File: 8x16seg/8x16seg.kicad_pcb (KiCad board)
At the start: 4 copper layers, 162.2 x 30.5 mm, 76 parts, among them P1 CONN_01X08, P2 CONN_01X08, U1 TLC59282_REV, U2 TLC59282_REV, U3 TLC59282_REV, U4 TLC59282_REV, U5 TLC59282_REV, U6 TLC59282_REV, U7 TLC59282_REV, U8 TLC59282_REV, U9 TLC59282_REV

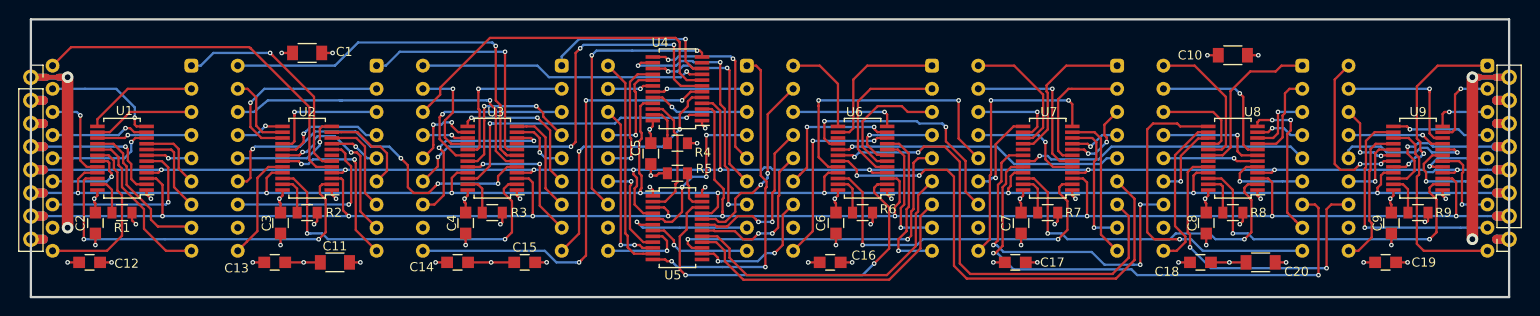
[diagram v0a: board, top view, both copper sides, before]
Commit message: Update LED module footprint to point to the 3D model.
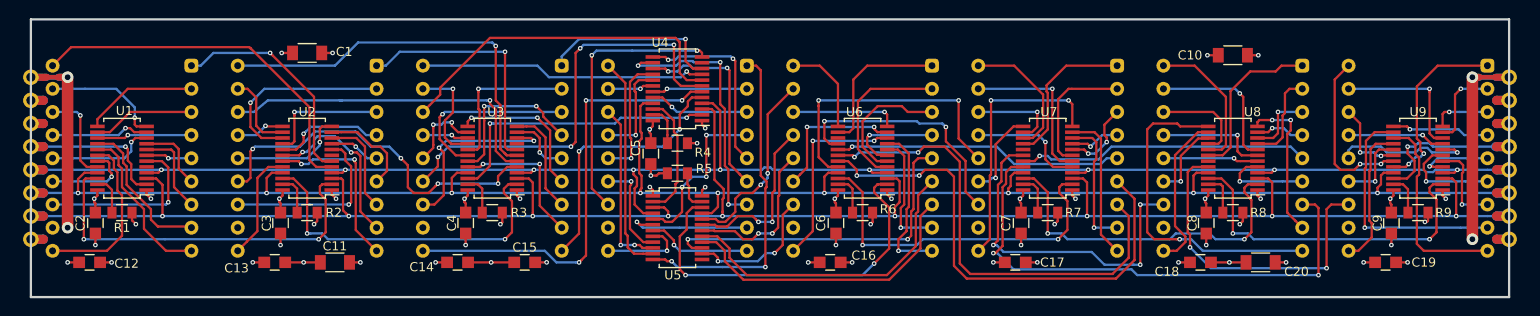
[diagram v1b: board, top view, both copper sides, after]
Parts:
- removed the REF** at (227.1, 97.8) (x2)
- removed the REF** at (227.1, 100.3) (x2)
- removed the REF** at (227.1, 102.9) (x2)
- removed the REF** at (227.1, 105.4) (x2)
- removed the REF** at (227.1, 108.0) (x2)
- removed the REF** at (227.1, 110.5) (x2)
- removed the REF** at (67.6, 110.5) (x2)
- removed the REF** at (227.1, 95.2) (x2)
- removed the REF** at (67.6, 108.0) (x2)
- removed the REF** at (67.6, 105.4) (x2)
- removed the REF** at (67.6, 102.9) (x2)
- removed the REF** at (67.6, 100.3) (x2)
- removed the REF** at (67.6, 97.8) (x2)
- added REF**: TestPoint_Pad_D1.0mm, TestPoint:TestPoint_Pad_D1.0mm, B.Cu at (227.1, 97.8)
- added REF**: TestPoint_Pad_D1.0mm, TestPoint:TestPoint_Pad_D1.0mm, B.Cu at (227.1, 100.3)
- added REF**: TestPoint_Pad_D1.0mm, TestPoint:TestPoint_Pad_D1.0mm, B.Cu at (227.1, 102.9)
- added REF**: TestPoint_Pad_D1.0mm, TestPoint:TestPoint_Pad_D1.0mm, B.Cu at (227.1, 105.4)
- added REF**: TestPoint_Pad_D1.0mm, TestPoint:TestPoint_Pad_D1.0mm, B.Cu at (227.1, 108.0)
- added REF**: TestPoint_Pad_D1.0mm, TestPoint:TestPoint_Pad_D1.0mm, B.Cu at (227.1, 110.5)
- added REF**: TestPoint_Pad_D1.0mm, TestPoint:TestPoint_Pad_D1.0mm, F.Cu at (227.1, 110.5)
- added REF**: TestPoint_Pad_D1.0mm, TestPoint:TestPoint_Pad_D1.0mm, F.Cu at (227.1, 108.0)
- added REF**: TestPoint_Pad_D1.0mm, TestPoint:TestPoint_Pad_D1.0mm, F.Cu at (227.1, 105.4)
- added REF**: TestPoint_Pad_D1.0mm, TestPoint:TestPoint_Pad_D1.0mm, F.Cu at (227.1, 102.9)
- added REF**: TestPoint_Pad_D1.0mm, TestPoint:TestPoint_Pad_D1.0mm, B.Cu at (67.6, 110.5)
- added REF**: TestPoint_Pad_D1.0mm, TestPoint:TestPoint_Pad_D1.0mm, F.Cu at (227.1, 100.3)
- added REF**: TestPoint_Pad_D1.0mm, TestPoint:TestPoint_Pad_D1.0mm, F.Cu at (227.1, 97.8)
- added REF**: TestPoint_Pad_D1.0mm, TestPoint:TestPoint_Pad_D1.0mm, F.Cu at (227.1, 95.2)
- added REF**: TestPoint_Pad_D1.0mm, TestPoint:TestPoint_Pad_D1.0mm, F.Cu at (67.6, 110.5)
- added REF**: TestPoint_Pad_D1.0mm, TestPoint:TestPoint_Pad_D1.0mm, F.Cu at (67.6, 108.0)
- added REF**: TestPoint_Pad_D1.0mm, TestPoint:TestPoint_Pad_D1.0mm, F.Cu at (67.6, 105.4)
- added REF**: TestPoint_Pad_D1.0mm, TestPoint:TestPoint_Pad_D1.0mm, F.Cu at (67.6, 102.9)
- added REF**: TestPoint_Pad_D1.0mm, TestPoint:TestPoint_Pad_D1.0mm, F.Cu at (67.6, 100.3)
- added REF**: TestPoint_Pad_D1.0mm, TestPoint:TestPoint_Pad_D1.0mm, F.Cu at (67.6, 97.8)
- added REF**: TestPoint_Pad_D1.0mm, TestPoint:TestPoint_Pad_D1.0mm, B.Cu at (67.6, 108.0)
- added REF**: TestPoint_Pad_D1.0mm, TestPoint:TestPoint_Pad_D1.0mm, B.Cu at (67.6, 105.4)
- added REF**: TestPoint_Pad_D1.0mm, TestPoint:TestPoint_Pad_D1.0mm, B.Cu at (67.6, 102.9)
- added REF**: TestPoint_Pad_D1.0mm, TestPoint:TestPoint_Pad_D1.0mm, B.Cu at (67.6, 100.3)
- added REF**: TestPoint_Pad_D1.0mm, TestPoint:TestPoint_Pad_D1.0mm, B.Cu at (67.6, 97.8)
- added REF**: TestPoint_Pad_D1.0mm, TestPoint:TestPoint_Pad_D1.0mm, B.Cu at (227.1, 95.2)

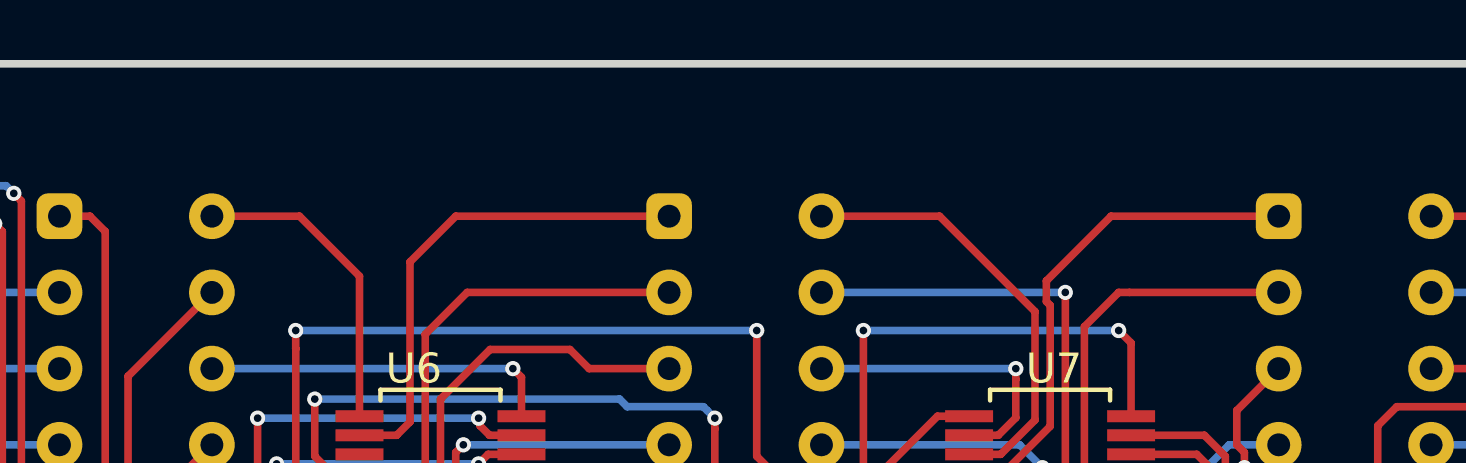
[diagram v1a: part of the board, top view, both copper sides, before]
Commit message: Add NC to unused pins.
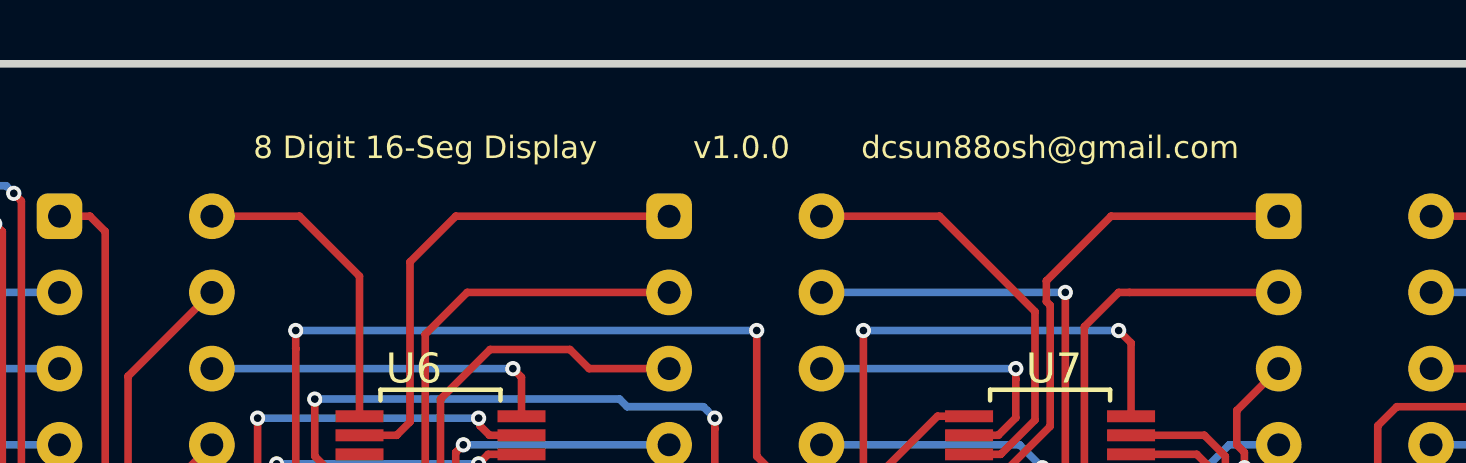
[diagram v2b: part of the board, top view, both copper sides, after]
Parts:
- removed the REF** at (227.1, 97.8) (x2)
- removed the REF** at (227.1, 100.3) (x2)
- removed the REF** at (227.1, 102.9) (x2)
- removed the REF** at (227.1, 105.4) (x2)
- removed the REF** at (227.1, 108.0) (x2)
- removed the REF** at (227.1, 110.5) (x2)
- removed the REF** at (67.6, 110.5) (x2)
- removed the REF** at (227.1, 95.2) (x2)
- removed the REF** at (67.6, 108.0) (x2)
- removed the REF** at (67.6, 105.4) (x2)
- removed the REF** at (67.6, 102.9) (x2)
- removed the REF** at (67.6, 100.3) (x2)
- removed the REF** at (67.6, 97.8) (x2)
- added REF**: TestPoint_Pad_D1.0mm, TestPoint:TestPoint_Pad_D1.0mm, B.Cu at (227.1, 97.8)
- added REF**: TestPoint_Pad_D1.0mm, TestPoint:TestPoint_Pad_D1.0mm, B.Cu at (227.1, 100.3)
- added REF**: TestPoint_Pad_D1.0mm, TestPoint:TestPoint_Pad_D1.0mm, B.Cu at (227.1, 102.9)
- added REF**: TestPoint_Pad_D1.0mm, TestPoint:TestPoint_Pad_D1.0mm, B.Cu at (227.1, 105.4)
- added REF**: TestPoint_Pad_D1.0mm, TestPoint:TestPoint_Pad_D1.0mm, B.Cu at (227.1, 108.0)
- added REF**: TestPoint_Pad_D1.0mm, TestPoint:TestPoint_Pad_D1.0mm, B.Cu at (227.1, 110.5)
- added REF**: TestPoint_Pad_D1.0mm, TestPoint:TestPoint_Pad_D1.0mm, F.Cu at (227.1, 110.5)
- added REF**: TestPoint_Pad_D1.0mm, TestPoint:TestPoint_Pad_D1.0mm, F.Cu at (227.1, 108.0)
- added REF**: TestPoint_Pad_D1.0mm, TestPoint:TestPoint_Pad_D1.0mm, F.Cu at (227.1, 105.4)
- added REF**: TestPoint_Pad_D1.0mm, TestPoint:TestPoint_Pad_D1.0mm, F.Cu at (227.1, 102.9)
- added REF**: TestPoint_Pad_D1.0mm, TestPoint:TestPoint_Pad_D1.0mm, B.Cu at (67.6, 110.5)
- added REF**: TestPoint_Pad_D1.0mm, TestPoint:TestPoint_Pad_D1.0mm, F.Cu at (227.1, 100.3)
- added REF**: TestPoint_Pad_D1.0mm, TestPoint:TestPoint_Pad_D1.0mm, F.Cu at (227.1, 97.8)
- added REF**: TestPoint_Pad_D1.0mm, TestPoint:TestPoint_Pad_D1.0mm, F.Cu at (227.1, 95.2)
- added REF**: TestPoint_Pad_D1.0mm, TestPoint:TestPoint_Pad_D1.0mm, F.Cu at (67.6, 110.5)
- added REF**: TestPoint_Pad_D1.0mm, TestPoint:TestPoint_Pad_D1.0mm, F.Cu at (67.6, 108.0)
- added REF**: TestPoint_Pad_D1.0mm, TestPoint:TestPoint_Pad_D1.0mm, F.Cu at (67.6, 105.4)
- added REF**: TestPoint_Pad_D1.0mm, TestPoint:TestPoint_Pad_D1.0mm, F.Cu at (67.6, 102.9)
- added REF**: TestPoint_Pad_D1.0mm, TestPoint:TestPoint_Pad_D1.0mm, F.Cu at (67.6, 100.3)
- added REF**: TestPoint_Pad_D1.0mm, TestPoint:TestPoint_Pad_D1.0mm, F.Cu at (67.6, 97.8)
- added REF**: TestPoint_Pad_D1.0mm, TestPoint:TestPoint_Pad_D1.0mm, B.Cu at (67.6, 108.0)
- added REF**: TestPoint_Pad_D1.0mm, TestPoint:TestPoint_Pad_D1.0mm, B.Cu at (67.6, 105.4)
- added REF**: TestPoint_Pad_D1.0mm, TestPoint:TestPoint_Pad_D1.0mm, B.Cu at (67.6, 102.9)
- added REF**: TestPoint_Pad_D1.0mm, TestPoint:TestPoint_Pad_D1.0mm, B.Cu at (67.6, 100.3)
- added REF**: TestPoint_Pad_D1.0mm, TestPoint:TestPoint_Pad_D1.0mm, B.Cu at (67.6, 97.8)
- added REF**: TestPoint_Pad_D1.0mm, TestPoint:TestPoint_Pad_D1.0mm, B.Cu at (227.1, 95.2)
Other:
- board text added: "8 Digit 16-Seg Display"
- board text added: "dcsun88osh@gmail.com"
- board text added: "v1.0.0"
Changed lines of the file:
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@@
-(kicad_pcb (version 20171130) (host pcbnew "(5.1.4-7-g3f91db25d)")
+(kicad_pcb (version 20171130) (host pcbnew "(5.1.5)")
   (general
     (thickness 1.6)
-    (drawings 6)
+    (drawings 9)
     (tracks 1740)
     (zones 0)
@@
   )
   (page A4)
+  (title_block
+    (title "8 Digit 16-Segment Display")
+    (date 2019-12-12)
+    (rev v1.0.0)
+  )
   (layers
     (0 F.Cu signal)
@@
     )
   )
+  (gr_text dcsun88osh@gmail.com (at 177.8 89.154) (layer F.SilkS)
+    (effects (font (size 0.75 0.75) (thickness 0.15)))
+  )
+  (gr_text v1.0.0 (at 167.513 89.154) (layer F.SilkS)
+    (effects (font (size 0.75 0.75) (thickness 0.15)))
+  )
+  (gr_text "8 Digit 16-Seg Display" (at 156.972 89.154) (layer F.SilkS)
+    (effects (font (size 0.75 0.75) (thickness 0.15)))
+  )
   (gr_line (start 63.5 115.6) (end 232.41 115.6) (layer Cmts.User) (width 0.15))

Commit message: Regenerate gerbers for 8x16-segment display board.
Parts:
- removed the REF** at (227.1, 97.8) (x2)
- removed the REF** at (227.1, 100.3) (x2)
- removed the REF** at (227.1, 102.9) (x2)
- removed the REF** at (227.1, 105.4) (x2)
- removed the REF** at (227.1, 108.0) (x2)
- removed the REF** at (227.1, 110.5) (x2)
- removed the REF** at (67.6, 110.5) (x2)
- removed the REF** at (227.1, 95.2) (x2)
- removed the REF** at (67.6, 108.0) (x2)
- removed the REF** at (67.6, 105.4) (x2)
- removed the REF** at (67.6, 102.9) (x2)
- removed the REF** at (67.6, 100.3) (x2)
- removed the REF** at (67.6, 97.8) (x2)
- added REF**: TestPoint_Pad_D1.0mm, TestPoint:TestPoint_Pad_D1.0mm, B.Cu at (227.1, 97.8)
- added REF**: TestPoint_Pad_D1.0mm, TestPoint:TestPoint_Pad_D1.0mm, B.Cu at (227.1, 100.3)
- added REF**: TestPoint_Pad_D1.0mm, TestPoint:TestPoint_Pad_D1.0mm, B.Cu at (227.1, 102.9)
- added REF**: TestPoint_Pad_D1.0mm, TestPoint:TestPoint_Pad_D1.0mm, B.Cu at (227.1, 105.4)
- added REF**: TestPoint_Pad_D1.0mm, TestPoint:TestPoint_Pad_D1.0mm, B.Cu at (227.1, 108.0)
- added REF**: TestPoint_Pad_D1.0mm, TestPoint:TestPoint_Pad_D1.0mm, B.Cu at (227.1, 110.5)
- added REF**: TestPoint_Pad_D1.0mm, TestPoint:TestPoint_Pad_D1.0mm, F.Cu at (227.1, 110.5)
- added REF**: TestPoint_Pad_D1.0mm, TestPoint:TestPoint_Pad_D1.0mm, F.Cu at (227.1, 108.0)
- added REF**: TestPoint_Pad_D1.0mm, TestPoint:TestPoint_Pad_D1.0mm, F.Cu at (227.1, 105.4)
- added REF**: TestPoint_Pad_D1.0mm, TestPoint:TestPoint_Pad_D1.0mm, F.Cu at (227.1, 102.9)
- added REF**: TestPoint_Pad_D1.0mm, TestPoint:TestPoint_Pad_D1.0mm, B.Cu at (67.6, 110.5)
- added REF**: TestPoint_Pad_D1.0mm, TestPoint:TestPoint_Pad_D1.0mm, F.Cu at (227.1, 100.3)
- added REF**: TestPoint_Pad_D1.0mm, TestPoint:TestPoint_Pad_D1.0mm, F.Cu at (227.1, 97.8)
- added REF**: TestPoint_Pad_D1.0mm, TestPoint:TestPoint_Pad_D1.0mm, F.Cu at (227.1, 95.2)
- added REF**: TestPoint_Pad_D1.0mm, TestPoint:TestPoint_Pad_D1.0mm, F.Cu at (67.6, 110.5)
- added REF**: TestPoint_Pad_D1.0mm, TestPoint:TestPoint_Pad_D1.0mm, F.Cu at (67.6, 108.0)
- added REF**: TestPoint_Pad_D1.0mm, TestPoint:TestPoint_Pad_D1.0mm, F.Cu at (67.6, 105.4)
- added REF**: TestPoint_Pad_D1.0mm, TestPoint:TestPoint_Pad_D1.0mm, F.Cu at (67.6, 102.9)
- added REF**: TestPoint_Pad_D1.0mm, TestPoint:TestPoint_Pad_D1.0mm, F.Cu at (67.6, 100.3)
- added REF**: TestPoint_Pad_D1.0mm, TestPoint:TestPoint_Pad_D1.0mm, F.Cu at (67.6, 97.8)
- added REF**: TestPoint_Pad_D1.0mm, TestPoint:TestPoint_Pad_D1.0mm, B.Cu at (67.6, 108.0)
- added REF**: TestPoint_Pad_D1.0mm, TestPoint:TestPoint_Pad_D1.0mm, B.Cu at (67.6, 105.4)
- added REF**: TestPoint_Pad_D1.0mm, TestPoint:TestPoint_Pad_D1.0mm, B.Cu at (67.6, 102.9)
- added REF**: TestPoint_Pad_D1.0mm, TestPoint:TestPoint_Pad_D1.0mm, B.Cu at (67.6, 100.3)
- added REF**: TestPoint_Pad_D1.0mm, TestPoint:TestPoint_Pad_D1.0mm, B.Cu at (67.6, 97.8)
- added REF**: TestPoint_Pad_D1.0mm, TestPoint:TestPoint_Pad_D1.0mm, B.Cu at (227.1, 95.2)
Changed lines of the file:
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@@
-(kicad_pcb (version 20171130) (host pcbnew "(5.1.5)")
+(kicad_pcb (version 20171130) (host pcbnew "(5.1.5-1-g2528d3844)")
   (general
     (thickness 1.6)

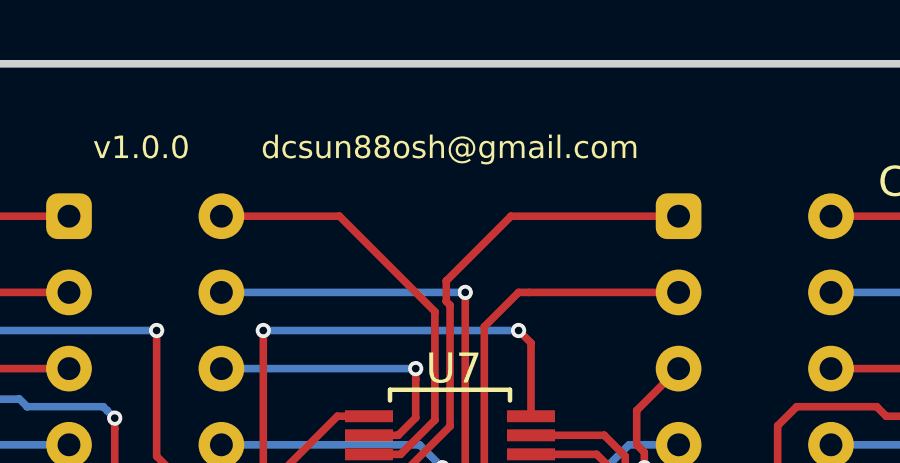
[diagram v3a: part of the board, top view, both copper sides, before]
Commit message: Update email address, regenerate gerber and plots. Change the sheet size of the clock power schematic page to A4.
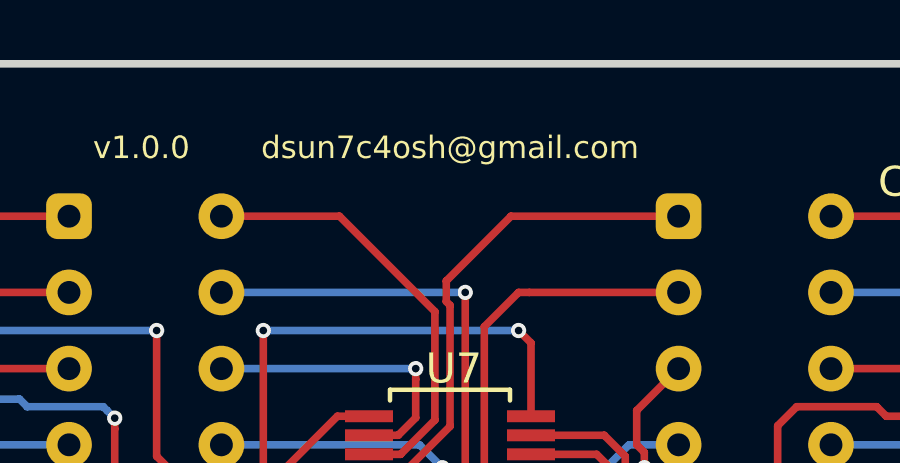
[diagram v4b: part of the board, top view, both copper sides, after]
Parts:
- removed the REF** at (227.1, 97.8) (x2)
- removed the REF** at (227.1, 100.3) (x2)
- removed the REF** at (227.1, 102.9) (x2)
- removed the REF** at (227.1, 105.4) (x2)
- removed the REF** at (227.1, 108.0) (x2)
- removed the REF** at (227.1, 110.5) (x2)
- removed the REF** at (67.6, 110.5) (x2)
- removed the REF** at (227.1, 95.2) (x2)
- removed the REF** at (67.6, 108.0) (x2)
- removed the REF** at (67.6, 105.4) (x2)
- removed the REF** at (67.6, 102.9) (x2)
- removed the REF** at (67.6, 100.3) (x2)
- removed the REF** at (67.6, 97.8) (x2)
- added REF**: TestPoint_Pad_D1.0mm, TestPoint:TestPoint_Pad_D1.0mm, B.Cu at (227.1, 97.8)
- added REF**: TestPoint_Pad_D1.0mm, TestPoint:TestPoint_Pad_D1.0mm, B.Cu at (227.1, 100.3)
- added REF**: TestPoint_Pad_D1.0mm, TestPoint:TestPoint_Pad_D1.0mm, B.Cu at (227.1, 102.9)
- added REF**: TestPoint_Pad_D1.0mm, TestPoint:TestPoint_Pad_D1.0mm, B.Cu at (227.1, 105.4)
- added REF**: TestPoint_Pad_D1.0mm, TestPoint:TestPoint_Pad_D1.0mm, B.Cu at (227.1, 108.0)
- added REF**: TestPoint_Pad_D1.0mm, TestPoint:TestPoint_Pad_D1.0mm, B.Cu at (227.1, 110.5)
- added REF**: TestPoint_Pad_D1.0mm, TestPoint:TestPoint_Pad_D1.0mm, F.Cu at (227.1, 110.5)
- added REF**: TestPoint_Pad_D1.0mm, TestPoint:TestPoint_Pad_D1.0mm, F.Cu at (227.1, 108.0)
- added REF**: TestPoint_Pad_D1.0mm, TestPoint:TestPoint_Pad_D1.0mm, F.Cu at (227.1, 105.4)
- added REF**: TestPoint_Pad_D1.0mm, TestPoint:TestPoint_Pad_D1.0mm, F.Cu at (227.1, 102.9)
- added REF**: TestPoint_Pad_D1.0mm, TestPoint:TestPoint_Pad_D1.0mm, B.Cu at (67.6, 110.5)
- added REF**: TestPoint_Pad_D1.0mm, TestPoint:TestPoint_Pad_D1.0mm, F.Cu at (227.1, 100.3)
- added REF**: TestPoint_Pad_D1.0mm, TestPoint:TestPoint_Pad_D1.0mm, F.Cu at (227.1, 97.8)
- added REF**: TestPoint_Pad_D1.0mm, TestPoint:TestPoint_Pad_D1.0mm, F.Cu at (227.1, 95.2)
- added REF**: TestPoint_Pad_D1.0mm, TestPoint:TestPoint_Pad_D1.0mm, F.Cu at (67.6, 110.5)
- added REF**: TestPoint_Pad_D1.0mm, TestPoint:TestPoint_Pad_D1.0mm, F.Cu at (67.6, 108.0)
- added REF**: TestPoint_Pad_D1.0mm, TestPoint:TestPoint_Pad_D1.0mm, F.Cu at (67.6, 105.4)
- added REF**: TestPoint_Pad_D1.0mm, TestPoint:TestPoint_Pad_D1.0mm, F.Cu at (67.6, 102.9)
- added REF**: TestPoint_Pad_D1.0mm, TestPoint:TestPoint_Pad_D1.0mm, F.Cu at (67.6, 100.3)
- added REF**: TestPoint_Pad_D1.0mm, TestPoint:TestPoint_Pad_D1.0mm, F.Cu at (67.6, 97.8)
- added REF**: TestPoint_Pad_D1.0mm, TestPoint:TestPoint_Pad_D1.0mm, B.Cu at (67.6, 108.0)
- added REF**: TestPoint_Pad_D1.0mm, TestPoint:TestPoint_Pad_D1.0mm, B.Cu at (67.6, 105.4)
- added REF**: TestPoint_Pad_D1.0mm, TestPoint:TestPoint_Pad_D1.0mm, B.Cu at (67.6, 102.9)
- added REF**: TestPoint_Pad_D1.0mm, TestPoint:TestPoint_Pad_D1.0mm, B.Cu at (67.6, 100.3)
- added REF**: TestPoint_Pad_D1.0mm, TestPoint:TestPoint_Pad_D1.0mm, B.Cu at (67.6, 97.8)
- added REF**: TestPoint_Pad_D1.0mm, TestPoint:TestPoint_Pad_D1.0mm, B.Cu at (227.1, 95.2)
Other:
- board text added: "dsun7c4osh@gmail.com"
- board text removed: "dcsun88osh@gmail.com"
